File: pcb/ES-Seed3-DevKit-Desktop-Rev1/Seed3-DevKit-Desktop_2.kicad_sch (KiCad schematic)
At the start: 48 parts, among them Q1 MMBT3904, Q2 MMBT3904, SW1 TOGGLE_ON_OFF_ON_PIP2, SW2 TOGGLE_ON-ON_PIP3, SW3 PTH Mini Button, SW4 PTH Mini Button, U11 H11L1, U7 MICRO_SD_CARD

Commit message: schematic is like 85% done.. just needs audio circuits, and opamp choice(s).
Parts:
- removed J_GATE_IN_2: ~, Electrosmith-Interface:S_JACK, symbol Electrosmith-Interface:EURO_JACK
- removed LED1: LED_RKBG, LED_THT:LED_D5.0mm-4_RGB_Wide_Pins, symbol Device:LED_RKBG
- removed Q2: MMBT3904, Package_TO_SOT_SMD:SOT-23, symbol Transistor_BJT:MMBT3904
- added LED10, LED11, LED12, LED13, LED14, LED15, LED16, LED2, LED3, LED4, LED5, LED6, LED7, LED8, LED9: LED, LED_THT:LED_D5.0mm, symbol Device:LED
- added R11, R12, R13, R14, R15, R16, R20, R21, R22, R26, R27: 10K, Resistor_SMD:R_0603_1608Metric, symbol Seed3-Pedal-DevKit-Converted-eagle-import:Electrosmith-Passives_R-US_R0603
- added R35, R36, R39, R41, R42, R45, R46, R47, R58, R69, R70, R71, R72, R74, R75: 2K, Resistor_SMD:R_0603_1608Metric, symbol Seed3-Pedal-DevKit-Converted-eagle-import:Electrosmith-Passives_R-US_R0603
- added SW10, SW11, SW12, SW13, SW14, SW15, SW16, SW3, SW4, SW5, SW6, SW7, SW8, SW9: PTH Mini Button, parts-for-kicad:TL1105SPF250Q_SILK, symbol parts-for-kicad:TAC_SWITCH_PTH_SILK
- added U8: PCA9685PW, Package_SO:TSSOP-28_4.4x9.7mm_P0.65mm, symbol Driver_LED:PCA9685PW
- R24: value 100K -> 10K
- R25: value 2K -> 10K
- R28: value 1M -> 10K
- R31: value 100R -> 10K
- renumbered LED2 to LED1, SW3 to SW1, SW2 to SW17, SW1 to SW18, SW4 to SW2
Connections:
- net +3V3: now also R24.2, R25.2, R28.2, R31.2, R11.2, R12.2, R13.2, R14.2, R15.2, R16.2, R20.2, R21.2, R22.2, R26.2, R27.2, R74.2, R75.2, U8.23 (~{OE}), U8.28 (VDD)
- net GND: now also LED10.1 (K), LED11.1 (K), LED12.1 (K), LED13.1 (K), LED14.1 (K), LED15.1 (K), LED16.1 (K), LED2.1 (K), LED3.1 (K), LED4.1 (K), LED5.1 (K), LED6.1 (K), LED7.1 (K), LED8.1 (K), LED9.1 (K), SW10.3, SW10.4, SW11.3, SW11.4, SW12.3, SW12.4, SW13.3, SW13.4, SW14.3, SW14.4, SW15.3, SW15.4, SW16.3, SW16.4, SW3.3, SW3.4, SW4.3, SW4.4, SW5.3, SW5.4, SW6.3, SW6.4, SW7.3, SW7.4, SW8.3, SW8.4, SW9.3, SW9.4, U8.1 (A0), U8.2 (A1), U8.24 (A5), U8.25 (EXTCLK), U8.3 (A2), U8.4 (A3), U8.5 (A4); no longer R28.1
- net TAC_SW1: now also R11.1
- net TAC_SW2: now also R12.1
- net TAC_SW12: now reaches R30.1
- net TAC_SW12: now also SW15.1, SW15.2; no longer R31.2
- net at R40.2: now also LED5.2 (A)
- net at R44.2: now also LED8.2 (A)
- net TAC_SW13: now reaches R24.1
- net TAC_SW13: now also SW10.1, SW10.2
- net GPIO_GATEIN_2 renamed TAC_SW16
- net TAC_SW16: now also SW16.1, SW16.2
- net LED_B renamed LED_8
- net LED_8: now also U8.13 (LED7)
- net LED_G renamed TAC_SW10
- net TAC_SW10: now also SW11.1, SW11.2
- net LED_MONO_1 renamed LED_1
- net LED_1: now also U8.6 (LED0)
- net LED_R renamed LED_5
- net LED_5: now also U8.10 (LED4)
- new net: LED6.2 (A), R41.2
- new net: LED7.2 (A), R42.2
- new net: LED15.2 (A), R71.2
- new net: LED10.2 (A), R46.2
- new net: LED4.2 (A), R39.2
- new net: LED13.2 (A), R69.2
- new net: LED2.2 (A), R35.2
- new net: LED3.2 (A), R36.2
- new net: LED9.2 (A), R45.2
- new net: LED16.2 (A), R72.2
- new net: LED12.2 (A), R58.2
- new net: LED14.2 (A), R70.2
- new net: LED11.2 (A), R47.2
- new net I2C_SCL: R74.1, U8.26 (SCL)
- new net I2C_SDA: R75.1, U8.27 (SDA)
- new net LED_10: R46.1, U8.16 (LED9)
- new net LED_11: R47.1, U8.17 (LED10)
- new net LED_12: R58.1, U8.18 (LED11)
- new net LED_13: R69.1, U8.19 (LED12)
- new net LED_14: R70.1, U8.20 (LED13)
- new net LED_15: R71.1, U8.21 (LED14)
- new net LED_16: R72.1, U8.22 (LED15)
- new net LED_2: R35.1, U8.7 (LED1)
- new net LED_3: R36.1, U8.8 (LED2)
- new net LED_4: R39.1, U8.9 (LED3)
- new net LED_6: R41.1, U8.11 (LED5)
- new net LED_7: R42.1, U8.12 (LED6)
- new net LED_9: R45.1, U8.15 (LED8)
- new net TAC_SW11: R27.1, SW13.1, SW13.2
- new net TAC_SW14: R26.1, SW12.1, SW12.2
- new net TAC_SW15: R28.1, SW14.1, SW14.2
- new net TAC_SW3: R13.1, SW3.1, SW3.2
- new net TAC_SW4: R14.1, SW4.1, SW4.2
- new net TAC_SW5: R15.1, SW5.1, SW5.2
- new net TAC_SW6: R16.1, SW6.1, SW6.2
- new net TAC_SW7: R20.1, SW7.1, SW7.2
- new net TAC_SW8: R21.1, SW8.1, SW8.2
- new net TAC_SW9: R22.1, SW9.1, SW9.2
- no-connect marks 4 -> 3
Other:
- note added: "If you add additional LED Drivers on another board: You can run them along side these by setting the address pins to a different value!"
- moved on the sheet: J_GATE_IN_1, LED1, Q1, R17, R18, R19, R23, R43, R50, R51, R52, R53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

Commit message: sch complete (pending value changes to audio out circuit and ERC fixes), footprints set, ready for layout.
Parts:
- removed J_GATE_IN_1: ~, Electrosmith-Interface:S_JACK, symbol Electrosmith-Interface:EURO_JACK
- removed J_MIDI_IN1, J_MIDI_OUT1, J_MIDI_THRU1: ~, Electrosmith-Interface:STEREO_JACK_3.5MM, symbol Electrosmith-Interface:STEREO_JACK
- added C34: 100NF, Capacitor_SMD:C_0603_1608Metric, symbol Seed3-Pedal-DevKit-Converted-eagle-import:Electrosmith-Passives_C-EUC0402
- added J10, J11, J8: DIN_MIDI_5P, parts-for-kicad:57PC5F, symbol Seed3-Pedal-DevKit-Converted-eagle-import:DIN_MIDI_5P
- added J_GATE_IN1, J_GATE_IN2: ~, Electrosmith-Interface:S_JACK, symbol Electrosmith-Interface:EURO_JACK
- added Q2: MMBT3904, Package_TO_SOT_SMD:SOT-23, symbol Transistor_BJT:MMBT3904
- added R66: 100K, Resistor_SMD:R_0603_1608Metric, symbol Seed3-Pedal-DevKit-Converted-eagle-import:Electrosmith-Passives_R-US_R0603
- added R67: 1M, Resistor_SMD:R_0603_1608Metric, symbol Seed3-Pedal-DevKit-Converted-eagle-import:Electrosmith-Passives_R-US_R0603
- added R68: 10K, Resistor_SMD:R_0603_1608Metric, symbol Seed3-Pedal-DevKit-Converted-eagle-import:Electrosmith-Passives_R-US_R0603
- added R73: 100R, Resistor_SMD:R_0603_1608Metric, symbol Seed3-Pedal-DevKit-Converted-eagle-import:Electrosmith-Passives_R-US_R0603
- LED1, LED10, LED11, LED12, LED13, LED14, LED15, LED16, LED2, LED3, LED4, LED5, LED6, LED7, LED8, LED9: footprint LED_THT:LED_D5.0mm -> LED_SMD:LED_0603_1608Metric
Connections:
- net +3V3: now also R68.2
- net GND: now also C34.2, J11.GND1 (PE), J11.GND2 (PE), J11.P2 (2), J8.GND1 (PE), J8.GND2 (PE), J8.P2 (2), J_GATE_IN1.GND, J_GATE_IN2.GND, Q2.2 (E), R67.1
- net GPIO_GATEIN_1: now also R73.1
- net MIDI_IN_4: now also J10.P4 (4)
- net MIDI_IN_5: now also J10.P5 (5)
- net at R10.1: now also J8.P4 (4)
- net SDMMC_DETECT: now reaches U7.CD1 (CD)
- net at C47.1: now also J10.GND1 (PE), J10.GND2 (PE)
- net at R29.2: now also J8.P5 (5)
- net at R6.1: now also J11.P4 (4)
- net at R59.2: now also J11.P5 (5)
- net at R17.1: now also J_GATE_IN1.TIP
- new net: C34.1, J10.P2 (2)
- new net: J_GATE_IN2.TIP, R66.1
- new net: Q2.1 (B), R66.2, R67.2
- new net: Q2.3 (C), R68.1, R73.2
- no-connect marks 3 -> 9
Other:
- note added: "MIDI IN"
- note added: "MIDI OUT"
- note added: "MIDI THRU"
- note removed: "IN"
- note removed: "OUT"
- note removed: "THRU"
- moved on the sheet: C1, C47, Q1, R17, R18, R19, R23, R29, R3, R4, R50, R51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

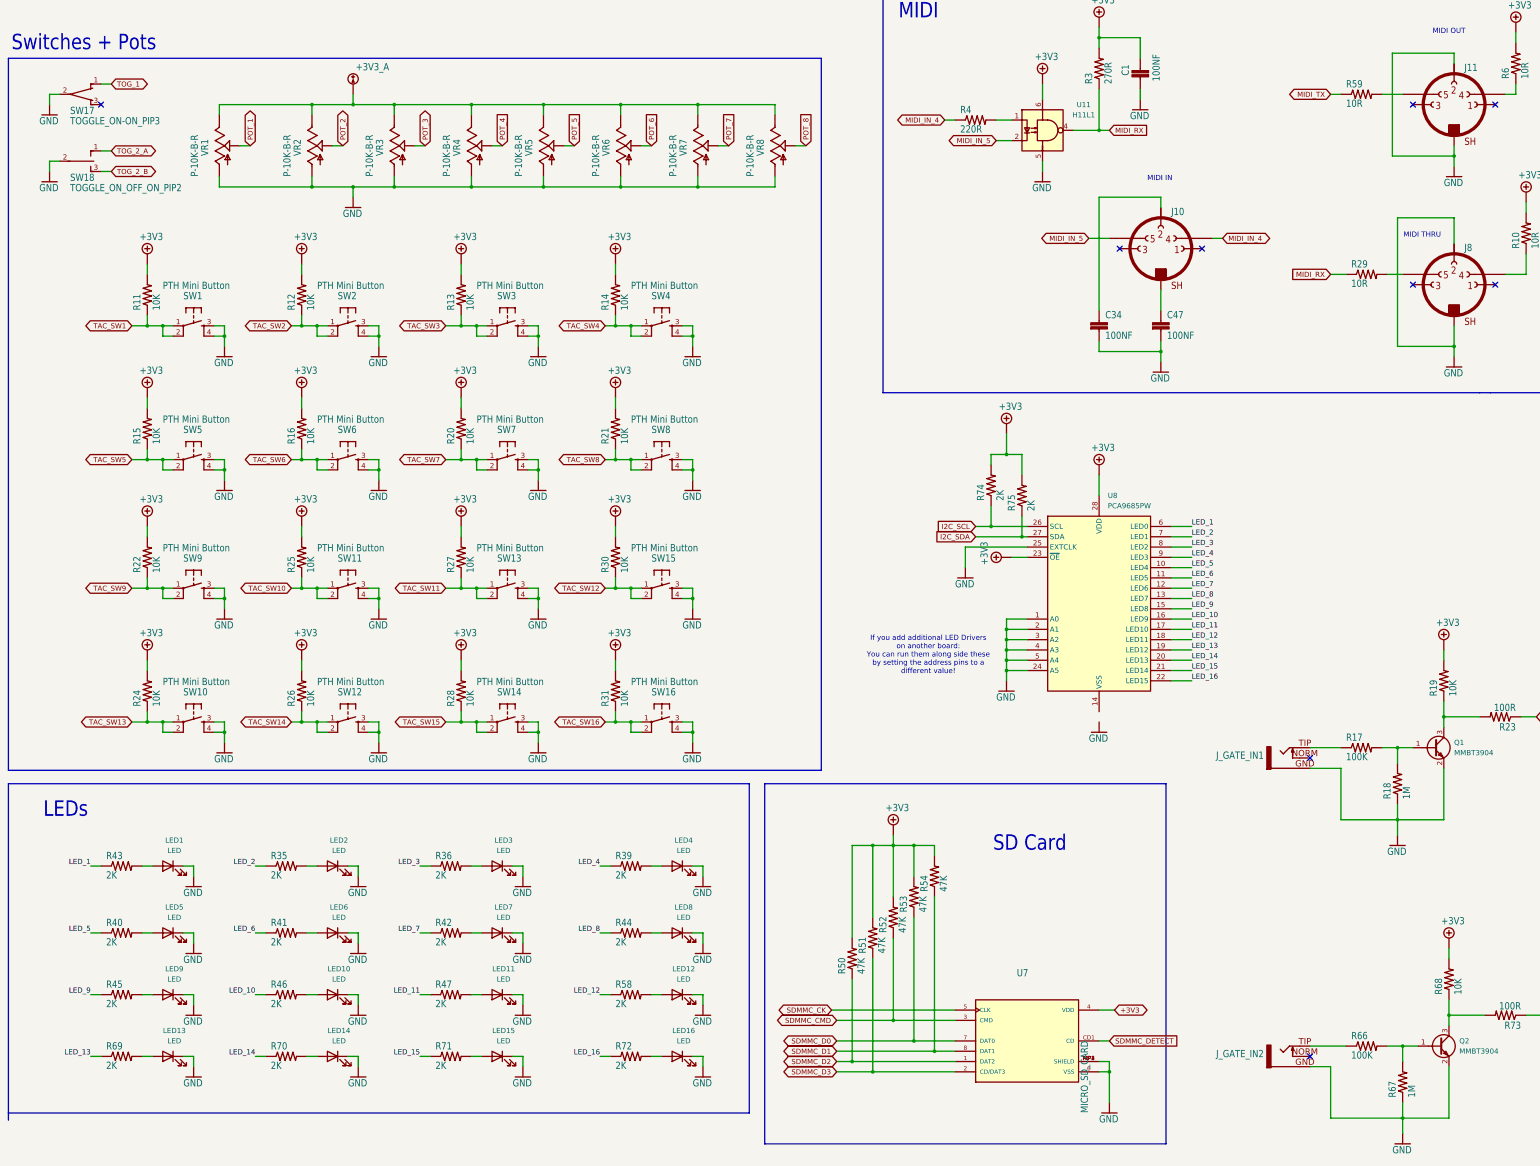
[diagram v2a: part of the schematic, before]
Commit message: lsno ERC errors or warnings, the few leftover warnings are excluded with valid comments.
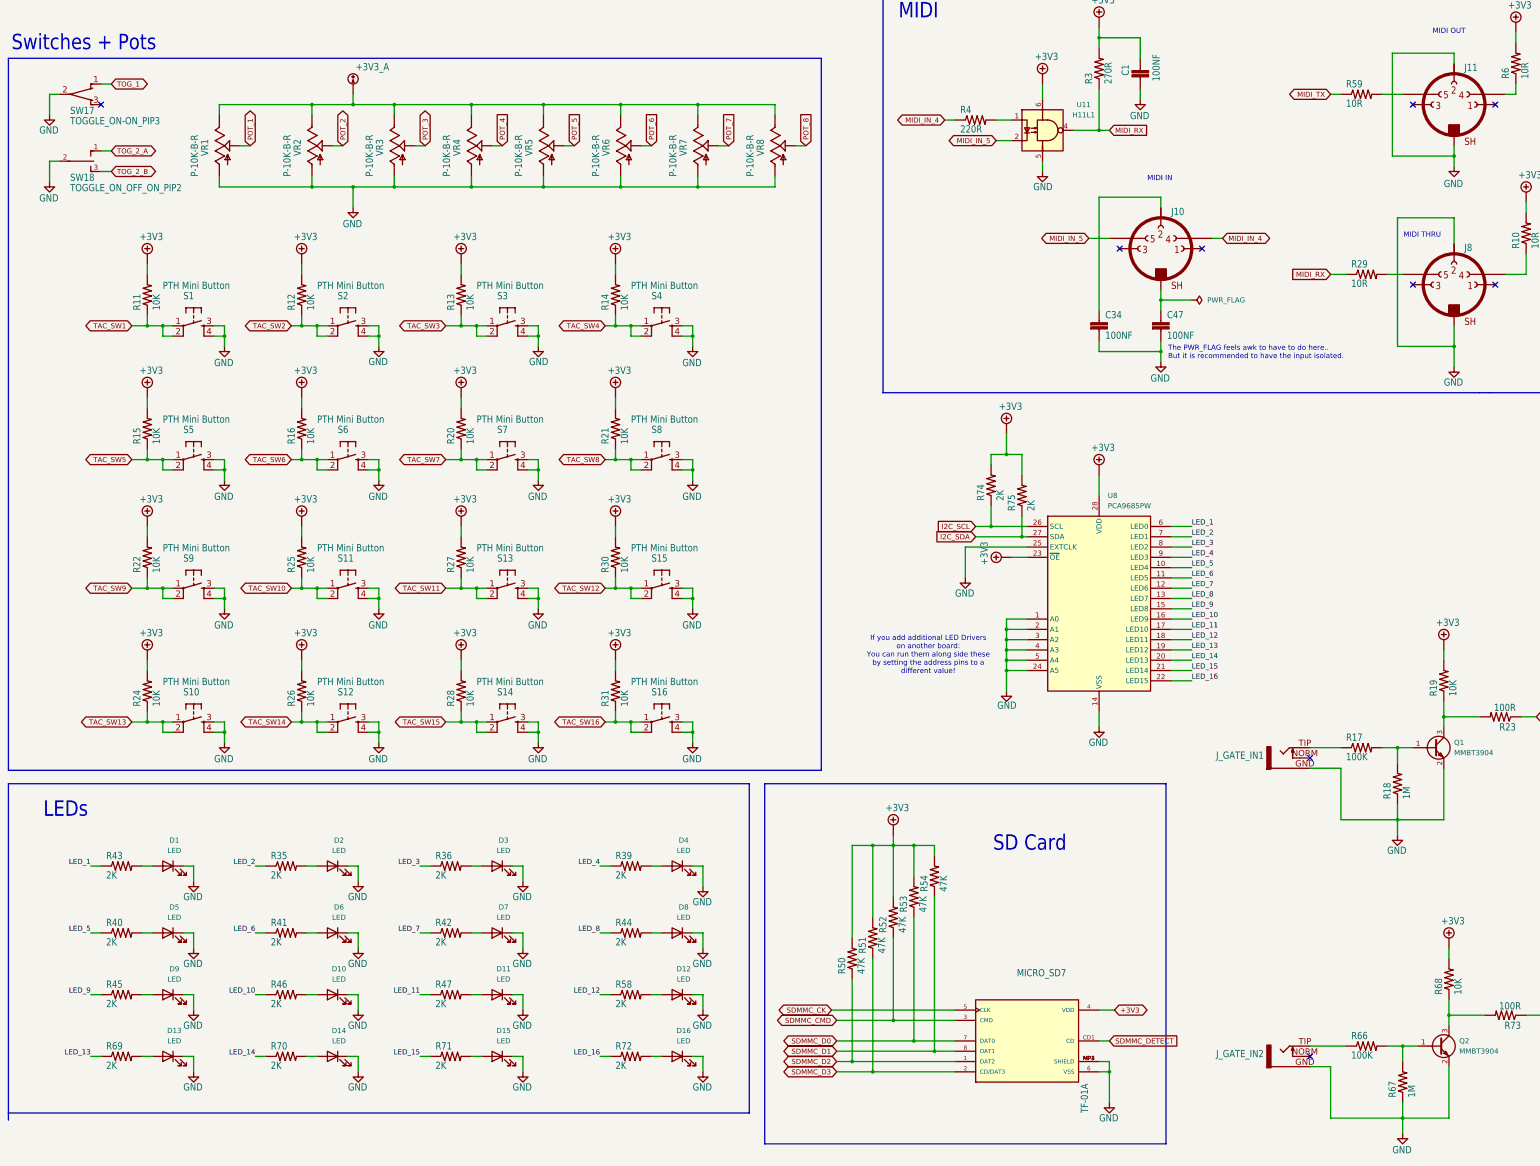
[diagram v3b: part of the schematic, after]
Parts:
- MICRO_SD7: renamed from U7; value MICRO_SD_CARD -> TF-01A; Description_1 Standard Card Edge Connectors -> Standard Card Edge Connectors
- SW17: footprint parts-for-kicad:TOGGLE_ON-ON_SILK -> parts-for-kicad:TOGGLE_SILK_PIP3
- SW18: footprint parts-for-kicad:TOGGLE_ON_OFF_ON_SILK -> Electrosmith-Interface:TOGGLE_ON_OFF_ON
- renumbered LED1 to D1, LED10 to D10, LED11 to D11, LED12 to D12, LED13 to D13, LED14 to D14, LED15 to D15, LED16 to D16, LED2 to D2, LED3 to D3, LED4 to D4, LED5 to D5, LED6 to D6, LED7 to D7, LED8 to D8, LED9 to D9, SW1 to S1, SW10 to S10, SW11 to S11, SW12 to S12, SW13 to S13, SW14 to S14, SW15 to S15, SW16 to S16, SW2 to S2, SW3 to S3, SW4 to S4, SW5 to S5, SW6 to S6, SW7 to S7, SW8 to S8, SW9 to S9
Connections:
- net GND: now also U8.14 (VSS)
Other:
- note added: "The PWR_FLAG feels awk to have to do here.. But it is recommended to have the input isolated."

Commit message: we've got a layout going
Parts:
- SW17: footprint parts-for-kicad:TOGGLE_SILK_PIP3 -> Electrosmith-Interface:TOGGLE_ON-ON
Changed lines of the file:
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@@
 			)
 		)
-		(property "Footprint" "parts-for-kicad:TOGGLE_SILK_PIP3"
+		(property "Footprint" "Electrosmith-Interface:TOGGLE_ON-ON"
 			(at 43.18 33.02 0)
 			(effects

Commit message: everything on the board -- some fine tuning necessary, and then ready to route.
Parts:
- renumbered S11 to S10, S13 to S11, S15 to S12, S10 to S13, S12 to S14, S14 to S15
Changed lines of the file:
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@@
 		(on_board yes)
 		(dnp no)
-		(property "Reference" "S15"
+		(property "Reference" "S12"
 			(at 184.15 148.59 0)
 			(effects
@@
 			(project "ES-Seed3-DevKit-Desktop-Rev1"
 				(path "/19edde5c-efb5-4a72-a9f3-fb5a3c99bba0/0fd2c796-fc28-4dbb-a19a-be32e6f577a0"
-					(reference "S15")
+					(reference "S12")
 					(unit 1)
 				)
@@
 		(on_board yes)
 		(dnp no)
-		(property "Reference" "S13"
+		(property "Reference" "S11"
 			(at 146.05 148.59 0)
 			(effects
@@
 			(project "ES-Seed3-DevKit-Desktop-Rev1"
 				(path "/19edde5c-efb5-4a72-a9f3-fb5a3c99bba0/0fd2c796-fc28-4dbb-a19a-be32e6f577a0"
-					(reference "S13")
+					(reference "S11")
 					(unit 1)
 				)
@@
 		(on_board yes)
 		(dnp no)
-		(property "Reference" "S11"
+		(property "Reference" "S10"
 			(at 106.68 148.59 0)
 			(effects
@@
 			(project "ES-Seed3-DevKit-Desktop-Rev1"
 				(path "/19edde5c-efb5-4a72-a9f3-fb5a3c99bba0/0fd2c796-fc28-4dbb-a19a-be32e6f577a0"
-					(reference "S11")
+					(reference "S10")
 					(unit 1)
 				)
@@
 		(on_board yes)
 		(dnp no)
-		(property "Reference" "S10"
+		(property "Reference" "S13"
 			(at 68.58 181.61 0)
 			(effects
@@
 			(project "ES-Seed3-DevKit-Desktop-Rev1"
 				(path "/19edde5c-efb5-4a72-a9f3-fb5a3c99bba0/0fd2c796-fc28-4dbb-a19a-be32e6f577a0"
-					(reference "S10")
+					(reference "S13")
 					(unit 1)
 				)
@@
 		(on_board yes)
 		(dnp no)
-		(property "Reference" "S12"
+		(property "Reference" "S14"
 			(at 106.68 181.61 0)
 			(effects
@@
 			(project "ES-Seed3-DevKit-Desktop-Rev1"
 				(path "/19edde5c-efb5-4a72-a9f3-fb5a3c99bba0/0fd2c796-fc28-4dbb-a19a-be32e6f577a0"
-					(reference "S12")
+					(reference "S14")
 					(unit 1)
 				)
@@
 		(on_board yes)
 		(dnp no)
-		(property "Reference" "S14"
+		(property "Reference" "S15"
 			(at 146.05 181.61 0)
 			(effects
@@
 			(project "ES-Seed3-DevKit-Desktop-Rev1"
 				(path "/19edde5c-efb5-4a72-a9f3-fb5a3c99bba0/0fd2c796-fc28-4dbb-a19a-be32e6f577a0"
-					(reference "S14")
+					(reference "S15")
 					(unit 1)
 				)

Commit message: routed, productions mats, etc.
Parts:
- added C32: 100NF, Capacitor_SMD:C_0603_1608Metric, symbol Seed3-Pedal-DevKit-Converted-eagle-import:Electrosmith-Passives_C-EUC0402
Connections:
- net +3V3: now also C32.2
- net GND: now also C32.1
- net GPIO_GATEIN_1: no longer R73.1
- new net GPIO_GATEIN_2: R73.1
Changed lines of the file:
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@@
 	)
 	(junction
+		(at 294.64 129.54)
+		(diameter 0)
+		(color 0 0 0 0)
+	)
+	(junction
 		(at 97.79 154.94)
 		(diameter 0)
@@
 		)
 	)
+	(wire
+		(pts
+			(xy 294.64 129.54) (xy 294.64 132.08)
+		)
+		(stroke
+			(width 0)
+			(type default)
+		)
+	)
 	(polyline
 		(pts
@@
 	(wire
 		(pts
+			(xy 304.8 129.54) (xy 294.64 129.54)
+		)
+		(stroke
+			(width 0)
+			(type default)
+		)
+	)
+	(wire
+		(pts
 			(xy 110.49 55.88) (xy 110.49 60.96)
 		)
@@
 	(wire
 		(pts
+			(xy 312.42 116.84) (xy 304.8 116.84)
+		)
+		(stroke
+			(width 0)
+			(type default)
+		)
+	)
+	(wire
+		(pts
 			(xy 152.4 270.51) (xy 152.4 274.32)
 		)
@@
 	(wire
 		(pts
+			(xy 304.8 116.84) (xy 304.8 129.54)
+		)
+		(stroke
+			(width 0)
+			(type default)
+		)
+	)
+	(wire
+		(pts
 			(xy 196.85 255.27) (xy 196.85 259.08)
 		)
@@
 	(wire
 		(pts
+			(xy 312.42 119.38) (xy 312.42 116.84)
+		)
+		(stroke
+			(width 0)
+			(type default)
+		)
+	)
+	(wire
+		(pts
 			(xy 312.42 147.32) (xy 317.5 147.32)
 		)
@@
 	(wire
 		(pts
+			(xy 312.42 127) (xy 312.42 129.54)
+		)
+		(stroke
+			(width 0)
+			(type default)
+		)
+	)
+	(wire
+		(pts
 			(xy 58.42 223.52) (xy 60.96 223.52)
 		)
@@
 	(wire
 		(pts
-			(xy 294.64 127) (xy 294.64 132.08)
+			(xy 294.64 127) (xy 294.64 129.54)
 		)
 		(stroke
@@
 		)
 	)
-	(global_label "GPIO_GATEIN_1"
+	(global_label "GPIO_GATEIN_2"
 		(shape input)
 		(at 403.86 260.35 0)
@@
 	)
 	(symbol
+		(lib_id "Seed3-Pedal-DevKit-Converted-eagle-import:Electrosmith-Passives_C-EUC0402")
+		(at 312.42 124.46 180)
+		(unit 1)
+		(exclude_from_sim no)
+		(in_bom yes)
+		(on_board yes)
+		(dnp no)
+		(property "Reference" "C32"
+			(at 307.721 120.904 90)
+			(effects
+				(font
+					(size 1.778 1.5113)
+				)
+				(justify left bottom)
+			)
+		)
+		(property "Value" "100NF"
+			(at 315.341 118.364 90)
+			(effects
+				(font
+					(size 1.778 1.5113)
+				)
+				(justify left bottom)
+			)
+		)
+		(property "Footprint" "Capacitor_SMD:C_0603_1608Metric"
+			(at 312.42 124.46 0)
+			(effects
+				(font
+					(size 1.27 1.27)
+				)
+				(hide yes)
+			)
+		)
+		(property "Datasheet" ""
+			(at 312.42 124.46 0)
+			(effects
+				(font
+					(size 1.27 1.27)
+				)
+				(hide yes)
+			)
+		)
+		(property "Description" ""
+			(at 312.42 124.46 0)
+			(effects
+				(font
+					(size 1.27 1.27)
+				)
+				(hide yes)
+			)
+		)
+		(pin "1"
+		)
+		(pin "2"
+		)
+		(instances
+			(project "ES-Seed3-DevKit-Desktop-Rev1"
+				(path "/19edde5c-efb5-4a72-a9f3-fb5a3c99bba0/0fd2c796-fc28-4dbb-a19a-be32e6f577a0"
+					(reference "C32")
+					(unit 1)
+				)
+			)
+		)
+	)
+	(symbol
 		(lib_id "Seed3-Pedal-DevKit-Converted-eagle-import:Electrosmith-Passives_R-US_R0603")
 		(at 393.7 186.69 180)
@@
 					(unit 1)
 				)
+			)
+		)
+	)
+	(symbol
+		(lib_id "power:GND")
+		(at 312.42 129.54 0)
+		(unit 1)
+		(exclude_from_sim no)
+		(in_bom yes)
+		(on_board yes)
+		(dnp no)
+		(property "Reference" "#GND089"
+			(at 312.42 129.54 0)
+			(effects
+				(font
+					(size 1.27 1.27)
+				)
+				(hide yes)
+			)
+		)
+		(property "Value" "GND"
+			(at 309.88 134.366 0)
+			(effects
+				(font
+					(size 1.778 1.5113)
+				)
+				(justify left bottom)
+			)
+		)
+		(property "Footprint" ""
+			(at 312.42 129.54 0)
+			(effects
+				(font
+					(size 1.27 1.27)
+				)
+				(hide yes)
+			)
+		)
+		(property "Datasheet" ""
+			(at 312.42 129.54 0)
+			(effects
+				(font
+					(size 1.27 1.27)
+				)
+				(hide yes)
+			)
+		)
+		(property "Description" "Power symbol creates a global label with name \"GND\" , ground"
+			(at 312.42 129.54 0)
+			(effects
+				(font
+					(size 1.27 1.27)
+				)
+				(hide yes)
+			)
+		)
+		(pin "1"
+		)
+		(instances
+			(project "ES-Seed3-DevKit-Desktop-Rev1"
+				(path "/19edde5c-efb5-4a72-a9f3-fb5a3c99bba0/0fd2c796-fc28-4dbb-a19a-be32e6f577a0"
+					(reference "#GND089")
+					(unit 1)
+				)
